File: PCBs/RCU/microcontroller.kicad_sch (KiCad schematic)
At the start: 26 parts

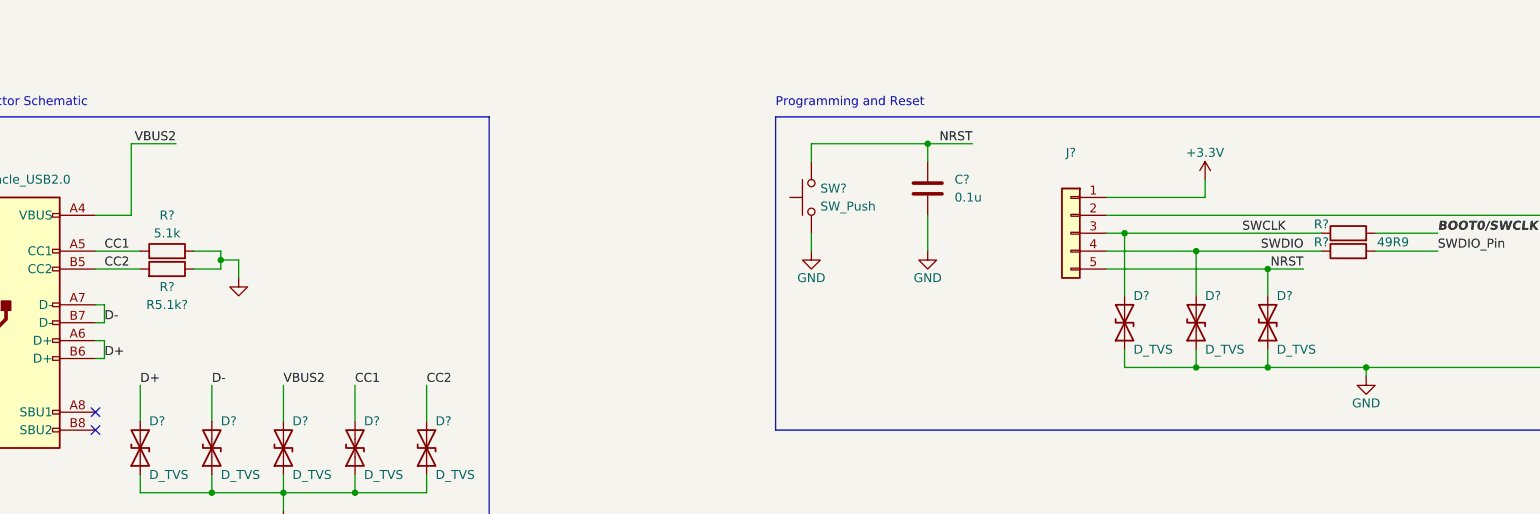
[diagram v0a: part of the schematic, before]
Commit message: Add USB power filter circuitry and corrected Motor Driver schematic
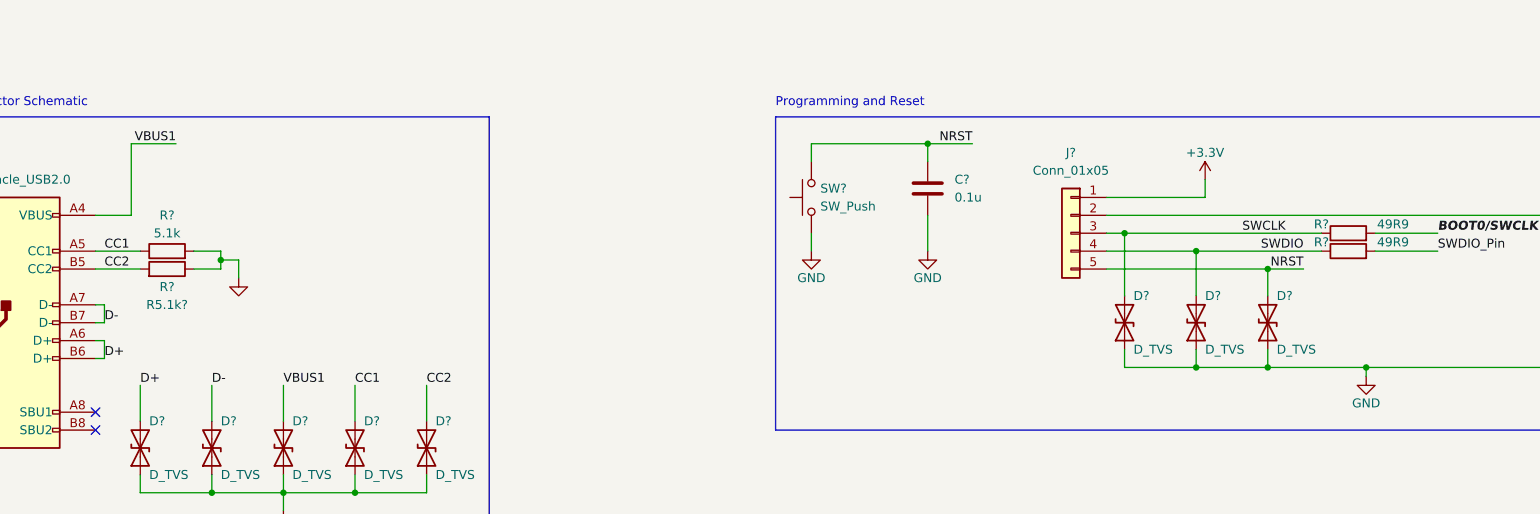
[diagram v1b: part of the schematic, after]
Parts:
- J?: value (none) -> Conn_01x05
- R?: value (none) -> 49R9
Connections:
- net VBUS2 renamed VBUS1
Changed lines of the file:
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@@
     (effects (font (size 1.27 1.27) (thickness 0.254) bold italic) (justify left bottom))
   )
-  (label "VBUS2" (at 81.28 153.67 0)
+  (label "VBUS1" (at 81.28 153.67 0)
     (effects (font (size 1.27 1.27)) (justify left bottom))
   )
@@
     (effects (font (size 1.27 1.27)) (justify right bottom))
   )
-  (label "VBUS2" (at 66.04 119.38 180)
+  (label "VBUS1" (at 66.04 119.38 180)
     (effects (font (size 1.27 1.27)) (justify right bottom))
   )
@@
     (in_bom yes) (on_board yes) (fields_autoplaced)
     (property "Reference" "J?" (id 0) (at 193.04 120.65 0))
-    (property "Value" "" (id 1) (at 193.04 123.19 0))
+    (property "Value" "Conn_01x05" (id 1) (at 193.04 123.19 0))
     (property "Footprint" "" (id 2) (at 193.04 132.08 0)
       (effects (font (size 1.27 1.27)) hide)
@@
     (in_bom yes) (on_board yes)
     (property "Reference" "R?" (id 0) (at 228.6 130.81 90))
-    (property "Value" "" (id 1) (at 238.76 130.81 90))
+    (property "Value" "49R9" (id 1) (at 238.76 130.81 90))
     (property "Footprint" "" (id 2) (at 232.41 133.858 90)
       (effects (font (size 1.27 1.27)) hide)

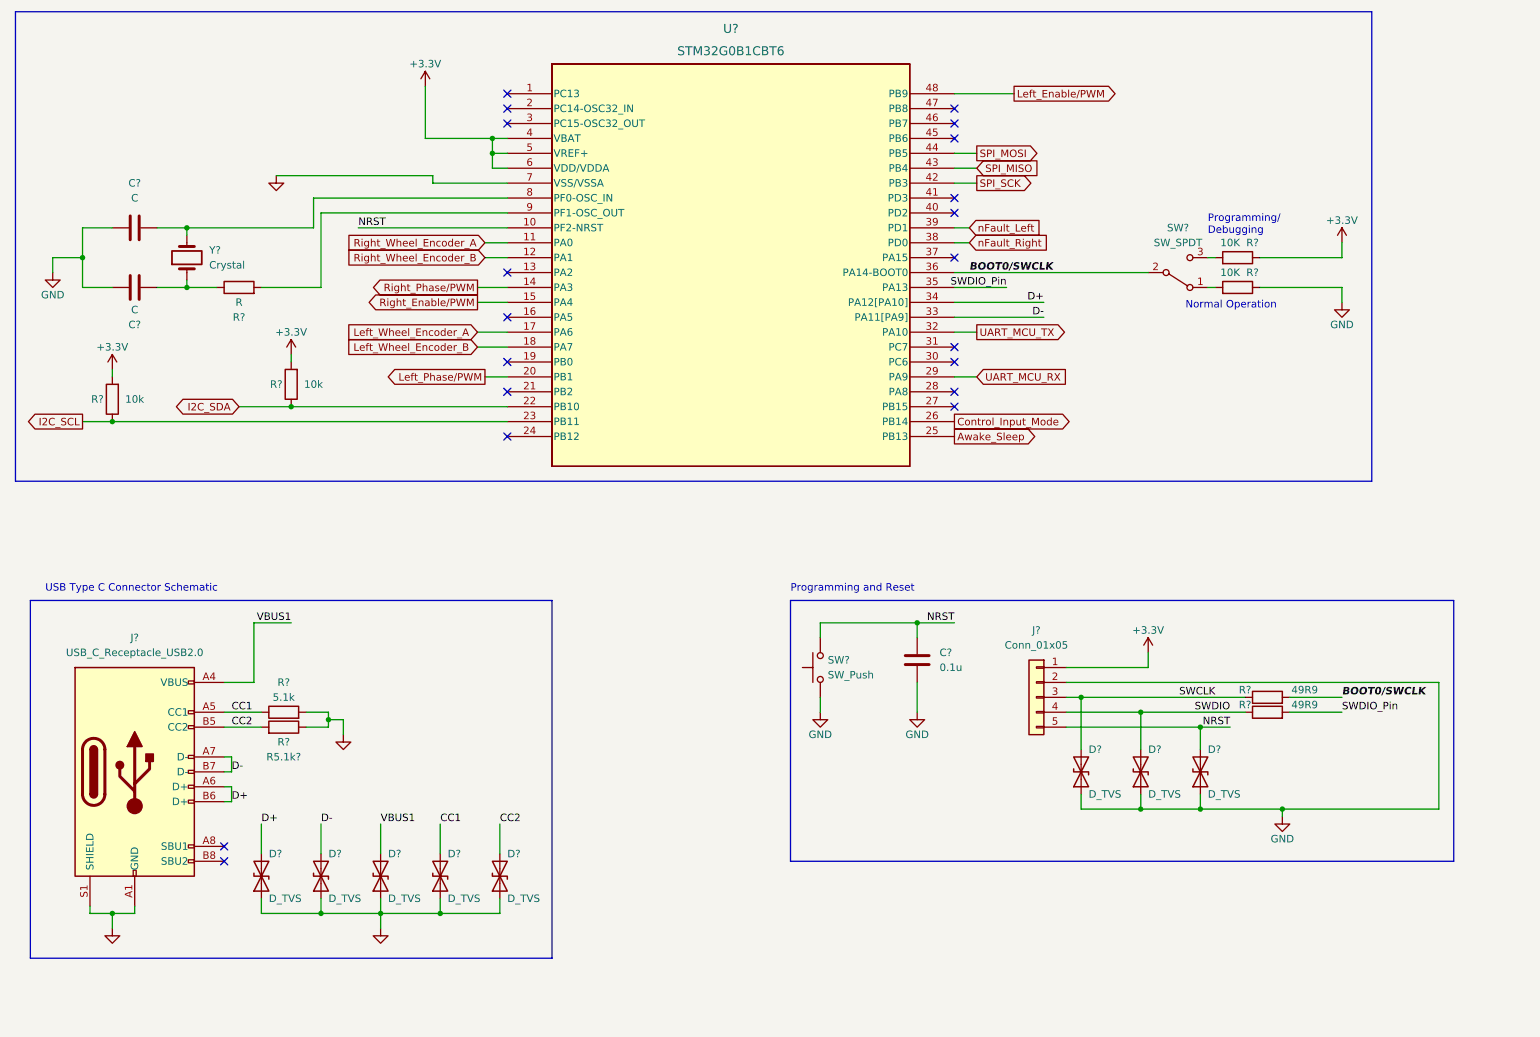
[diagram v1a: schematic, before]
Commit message: Numbered and ordered all of the modules
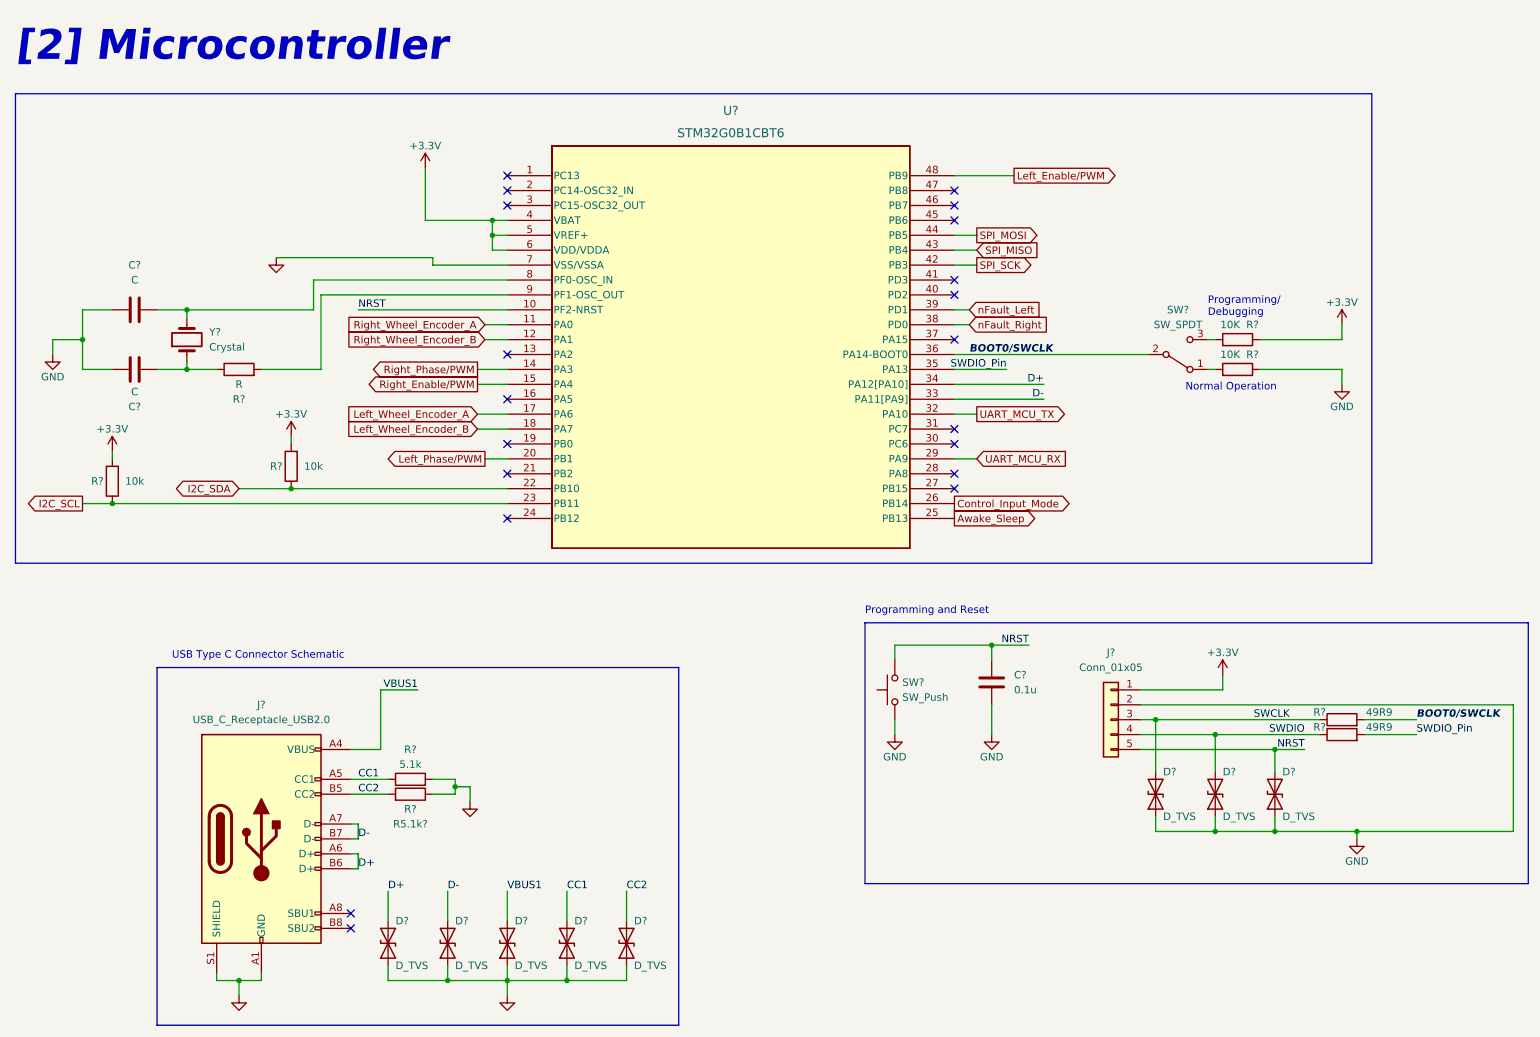
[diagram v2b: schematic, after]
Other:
- note added: "[2] Microcontroller"
- moved on the sheet: C?, D?, J?, R5.1k?, R?, SW?, U?, Y?
